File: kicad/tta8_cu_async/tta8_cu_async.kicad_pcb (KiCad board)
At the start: 4 copper layers, 92 x 100 mm, 23 parts, among them J1 Conn_02x32_Counter_Clockwise, J2 Conn_01x06, J3 Conn_02x02_Odd_Even, U1 74AHCT74, U10 74HCT193, U11 74HCT193, U12 74AHCT00, U13 74AHCT573, U14 74AHCT573, U15 74AHCT573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

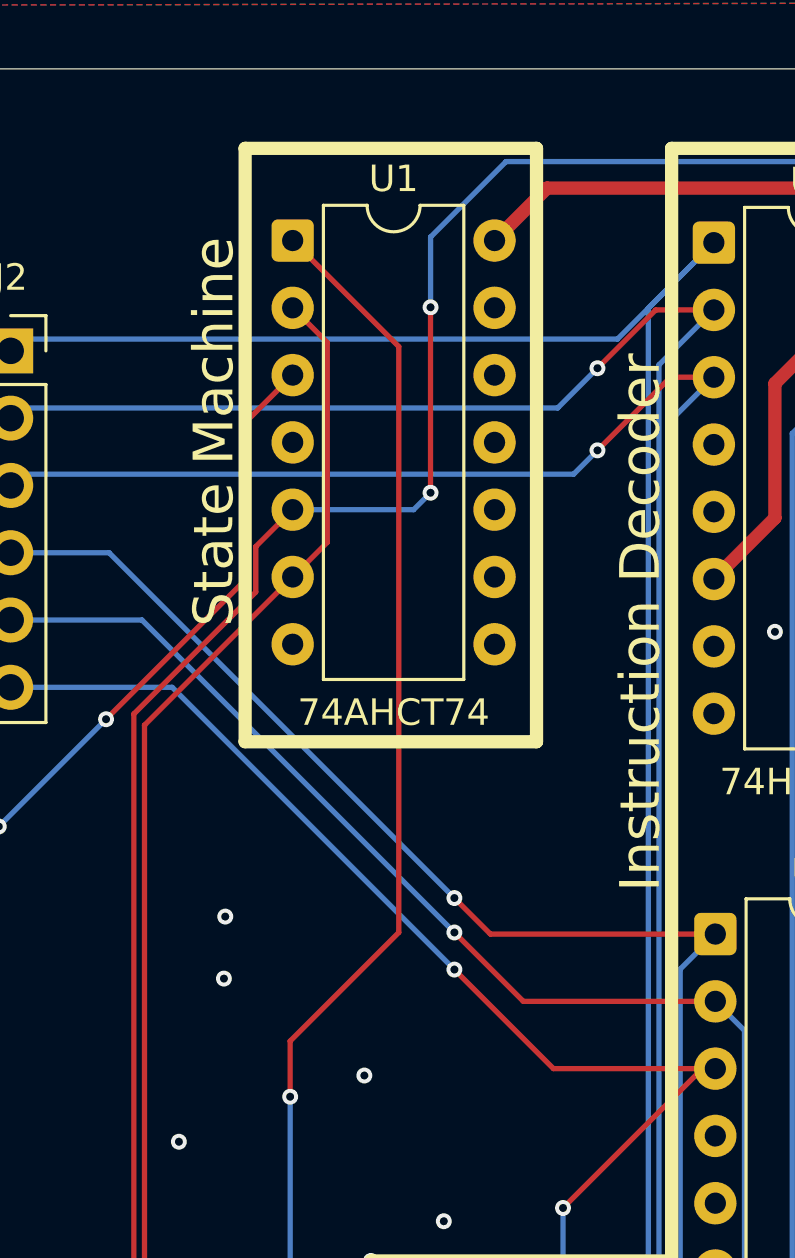
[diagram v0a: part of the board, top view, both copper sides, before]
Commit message: Fix floating /S in State Machine
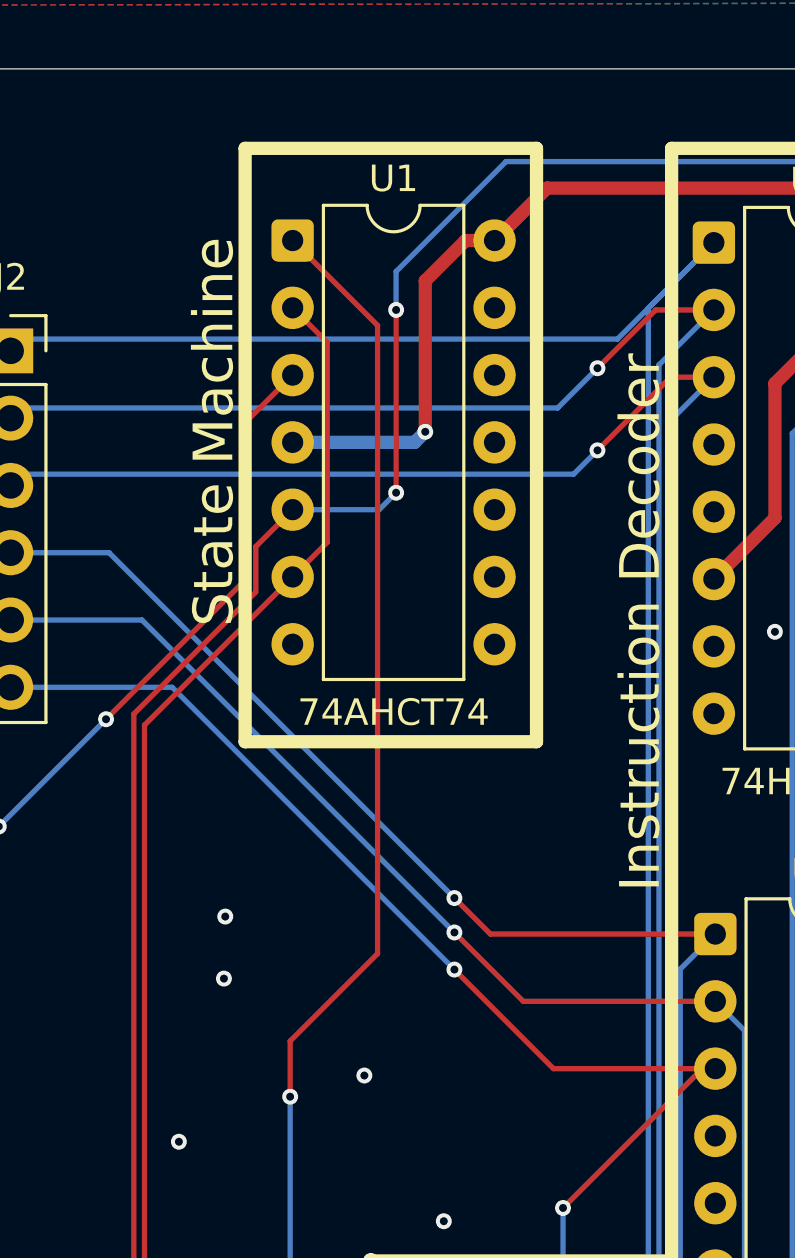
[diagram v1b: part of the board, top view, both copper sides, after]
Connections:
- U1 pad 4: unconnected-(U1A-~{S}-Pad4) -> +5V
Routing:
- net +5V: track 529.5 -> 543.6 mm, vias 0 -> 1
- net EXC: track 169.5 -> 168.7 mm
- net /R: track 100.7 -> 100.1 mm

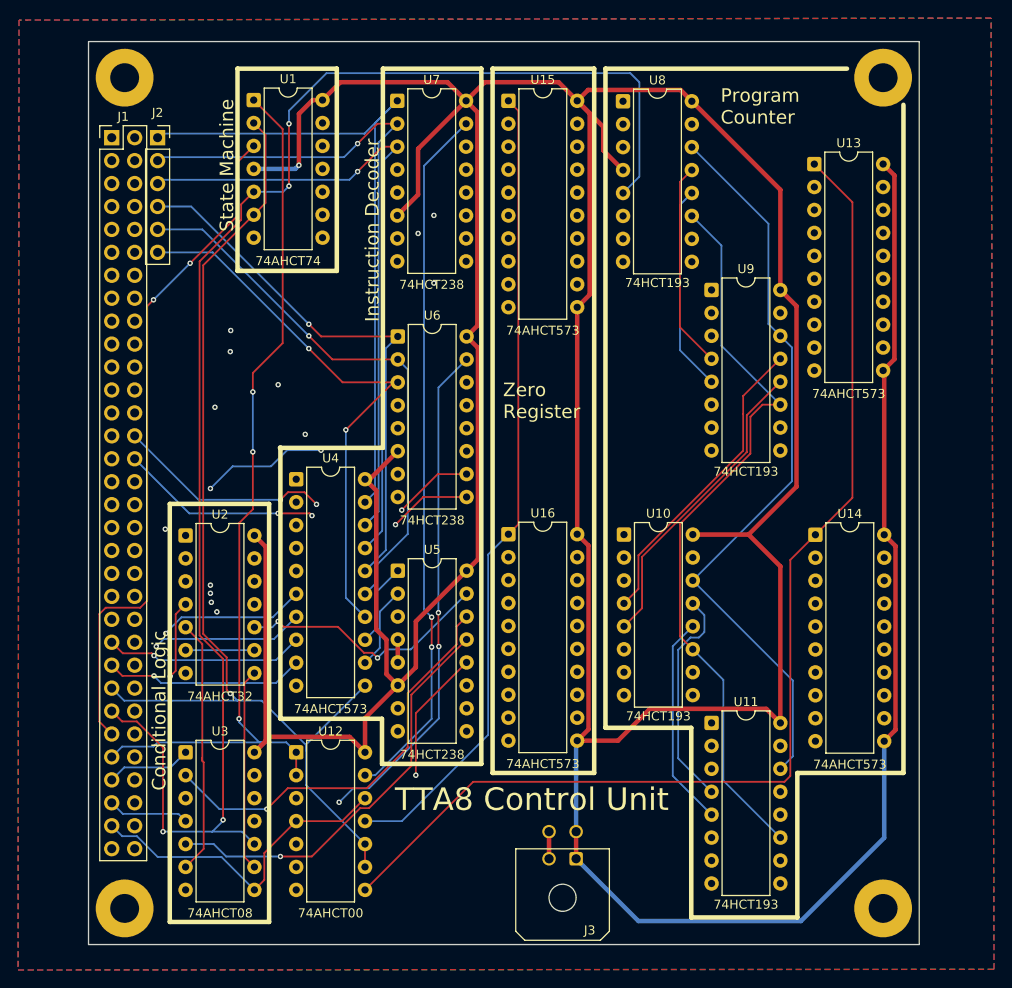
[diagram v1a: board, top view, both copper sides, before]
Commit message: cu change to sockets
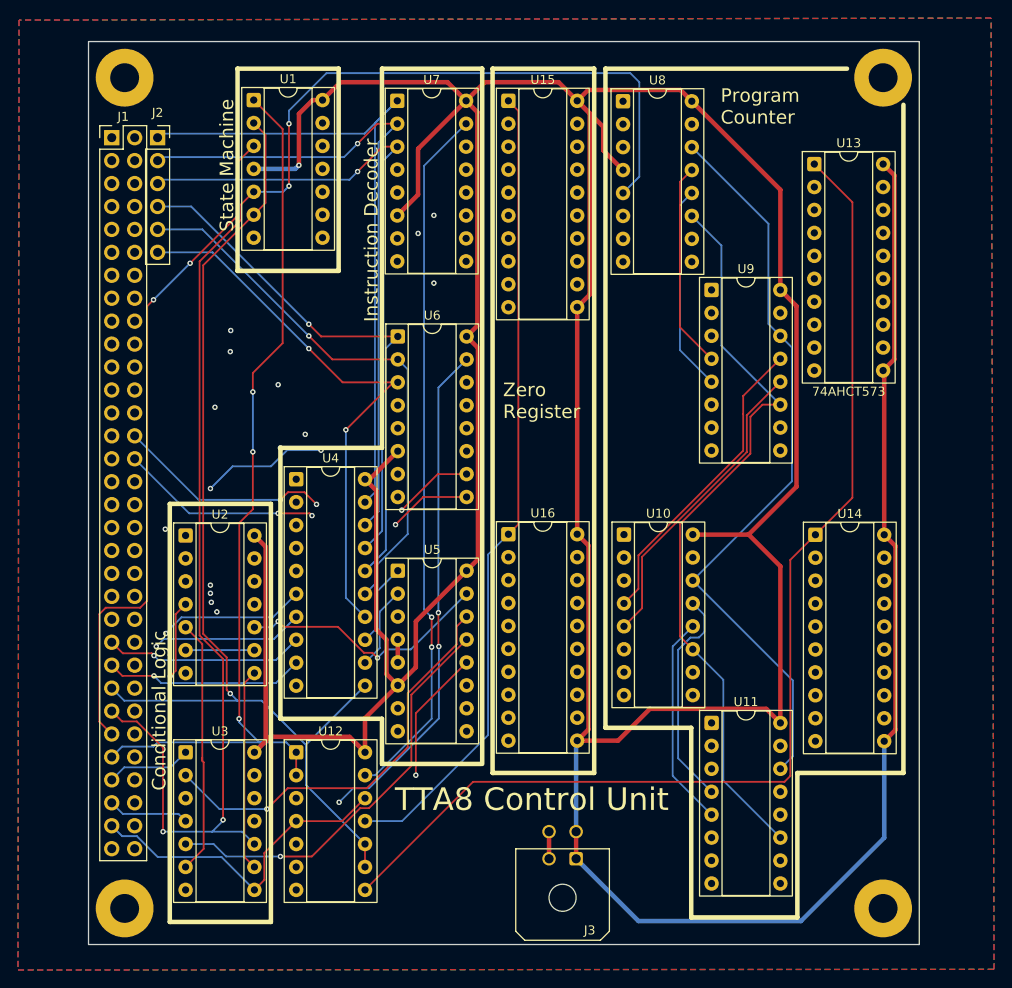
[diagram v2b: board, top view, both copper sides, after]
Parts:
- U1, U12, U2, U3: footprint Package_DIP:DIP-14_W7.62mm -> Package_DIP:DIP-14_W7.62mm_Socket
- U10, U11, U5, U6, U7, U8, U9: footprint Package_DIP:DIP-16_W7.62mm -> Package_DIP:DIP-16_W7.62mm_Socket
- U13, U14, U15, U16, U4: footprint Package_DIP:DIP-20_W7.62mm -> Package_DIP:DIP-20_W7.62mm_Socket
